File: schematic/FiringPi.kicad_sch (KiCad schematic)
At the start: 36 parts

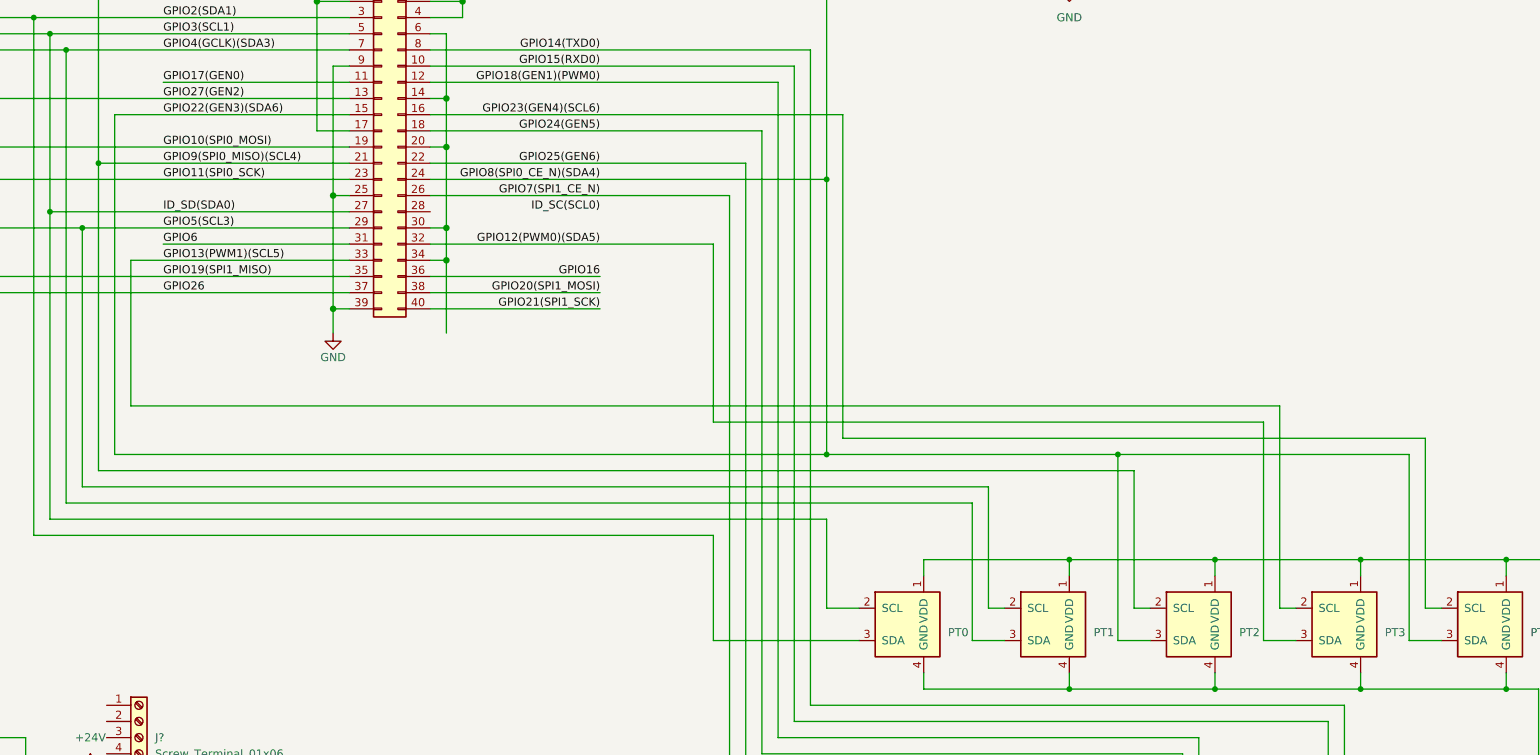
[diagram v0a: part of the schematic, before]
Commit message: ## week before hot fire - UI changes - corrected ordering of PTs - added readout for relay channel outputs
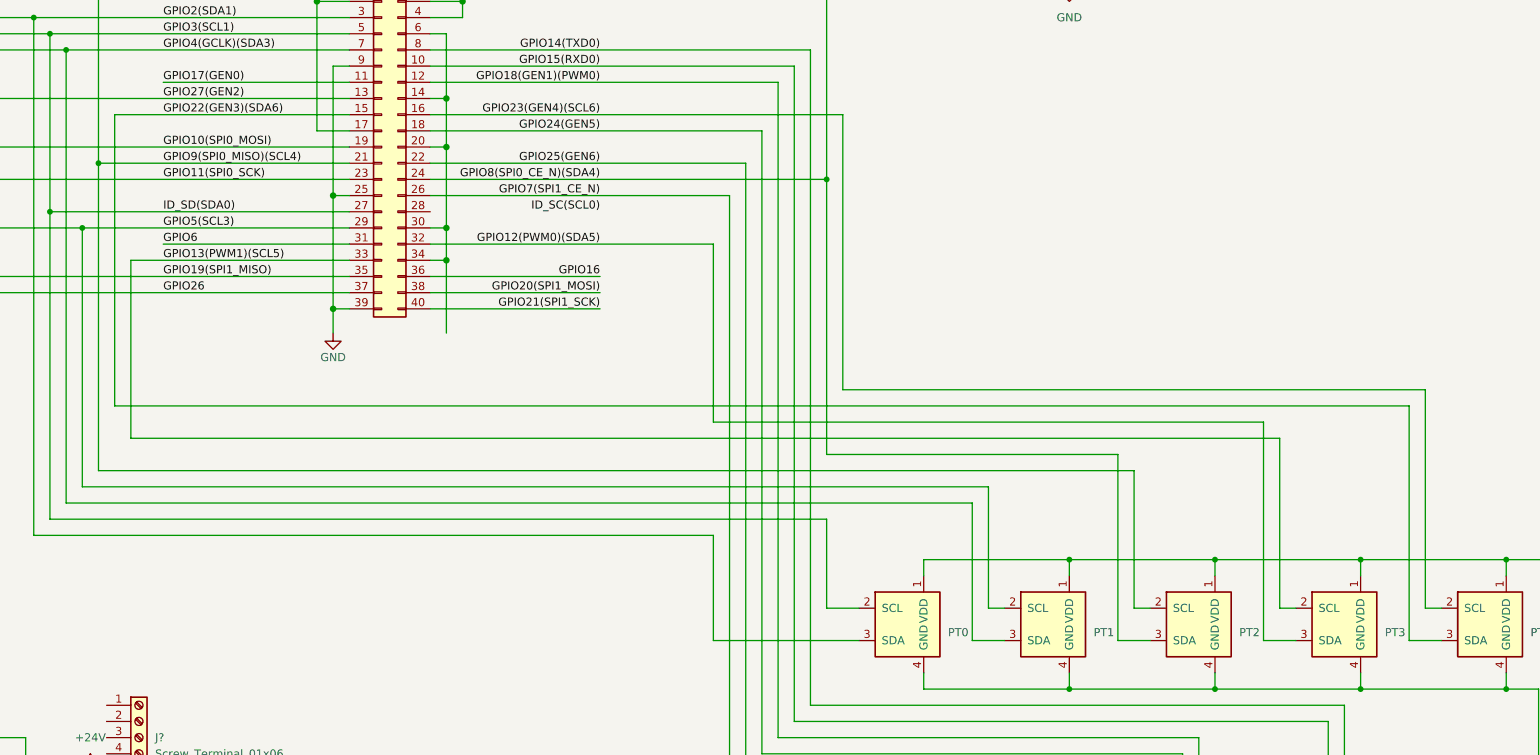
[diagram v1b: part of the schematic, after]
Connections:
- net GPIO22(GEN3)(SDA6): no longer P?.24 (Pin_24), U?.27 (SDA), U?.3 (SDA)
- new net GPIO8(SPI0_CE_N)(SDA4): P?.24 (Pin_24), U?.27 (SDA), U?.3 (SDA)
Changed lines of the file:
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@@
   (junction (at 353.06 40.64) (diameter 0) (color 0 0 0 0)
   )
-  (junction (at 261.62 167.64) (diameter 0) (color 0 0 0 0)
-  )
   (junction (at 373.38 237.49) (diameter 0) (color 0 0 0 0)
   )
@@
   (junction (at 26.67 104.14) (diameter 0) (color 0 0 0 0)
   )
-  (junction (at 307.34 167.64) (diameter 0) (color 0 0 0 0)
-  )
   (junction (at 299.72 184.15) (diameter 0) (color 0 0 0 0)
   )
@@
     (stroke (width 0) (type default) (color 0 0 0 0))
   )
+  (wire (pts (xy 149.86 160.02) (xy 353.06 160.02))
+    (stroke (width 0) (type default) (color 0 0 0 0))
+  )
   (wire (pts (xy 251.46 214.63) (xy 317.5 214.63))
     (stroke (width 0) (type default) (color 0 0 0 0))
@@
     (stroke (width 0) (type default) (color 0 0 0 0))
   )
-  (wire (pts (xy 149.86 114.3) (xy 149.86 167.64))
-    (stroke (width 0) (type default) (color 0 0 0 0))
-  )
   (wire (pts (xy 120.65 232.41) (xy 115.57 232.41))
     (stroke (width 0) (type default) (color 0 0 0 0))
@@
     (stroke (width 0) (type default) (color 0 0 0 0))
   )
-  (wire (pts (xy 264.16 165.1) (xy 264.16 114.3))
+  (wire (pts (xy 264.16 157.48) (xy 264.16 114.3))
     (stroke (width 0) (type default) (color 0 0 0 0))
   )
@@
     (stroke (width 0) (type default) (color 0 0 0 0))
   )
-  (wire (pts (xy 355.6 191.77) (xy 355.6 165.1))
+  (wire (pts (xy 355.6 191.77) (xy 355.6 157.48))
     (stroke (width 0) (type default) (color 0 0 0 0))
   )
@@
     (stroke (width 0) (type default) (color 0 0 0 0))
   )
-  (wire (pts (xy 353.06 167.64) (xy 353.06 196.85))
-    (stroke (width 0) (type default) (color 0 0 0 0))
-  )
   (wire (pts (xy 74.93 232.41) (xy 69.85 232.41))
     (stroke (width 0) (type default) (color 0 0 0 0))
@@
     (stroke (width 0) (type default) (color 0 0 0 0))
   )
-  (wire (pts (xy 355.6 165.1) (xy 264.16 165.1))
+  (wire (pts (xy 355.6 157.48) (xy 264.16 157.48))
     (stroke (width 0) (type default) (color 0 0 0 0))
   )
@@
     (stroke (width 0) (type default) (color 0 0 0 0))
   )
+  (wire (pts (xy 149.86 114.3) (xy 149.86 160.02))
+    (stroke (width 0) (type default) (color 0 0 0 0))
+  )
   (wire (pts (xy 373.38 204.47) (xy 368.3 204.47))
     (stroke (width 0) (type default) (color 0 0 0 0))
@@
     (stroke (width 0) (type default) (color 0 0 0 0))
   )
-  (wire (pts (xy 307.34 167.64) (xy 353.06 167.64))
-    (stroke (width 0) (type default) (color 0 0 0 0))
-  )
   (wire (pts (xy 87.63 209.55) (xy 87.63 212.09))
     (stroke (width 0) (type default) (color 0 0 0 0))
@@
     (stroke (width 0) (type default) (color 0 0 0 0))
   )
+  (wire (pts (xy 353.06 160.02) (xy 353.06 196.85))
+    (stroke (width 0) (type default) (color 0 0 0 0))
+  )
   (wire (pts (xy 71.12 90.17) (xy 74.93 90.17))
     (stroke (width 0) (type default) (color 0 0 0 0))
@@
     (stroke (width 0) (type default) (color 0 0 0 0))
   )
-  (wire (pts (xy 332.74 160.02) (xy 152.4 160.02))
+  (wire (pts (xy 332.74 165.1) (xy 152.4 165.1))
     (stroke (width 0) (type default) (color 0 0 0 0))
   )
@@
     (stroke (width 0) (type default) (color 0 0 0 0))
   )
-  (wire (pts (xy 152.4 160.02) (xy 152.4 137.16))
+  (wire (pts (xy 152.4 165.1) (xy 152.4 137.16))
     (stroke (width 0) (type default) (color 0 0 0 0))
   )
@@
     (stroke (width 0) (type default) (color 0 0 0 0))
   )
-  (wire (pts (xy 149.86 167.64) (xy 261.62 167.64))
-    (stroke (width 0) (type default) (color 0 0 0 0))
-  )
   (wire (pts (xy 358.14 63.5) (xy 334.01 63.5))
     (stroke (width 0) (type default) (color 0 0 0 0))
@@
     (stroke (width 0) (type default) (color 0 0 0 0))
   )
-  (wire (pts (xy 332.74 160.02) (xy 332.74 191.77))
-    (stroke (width 0) (type default) (color 0 0 0 0))
-  )
+  (wire (pts (xy 332.74 165.1) (xy 332.74 191.77))
+    (stroke (width 0) (type default) (color 0 0 0 0))
+  )
